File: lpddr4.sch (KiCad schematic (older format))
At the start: 90 parts, among them U1 MT53D1024M32D4DT-053, U3 MT53D1024M32D4DT-053

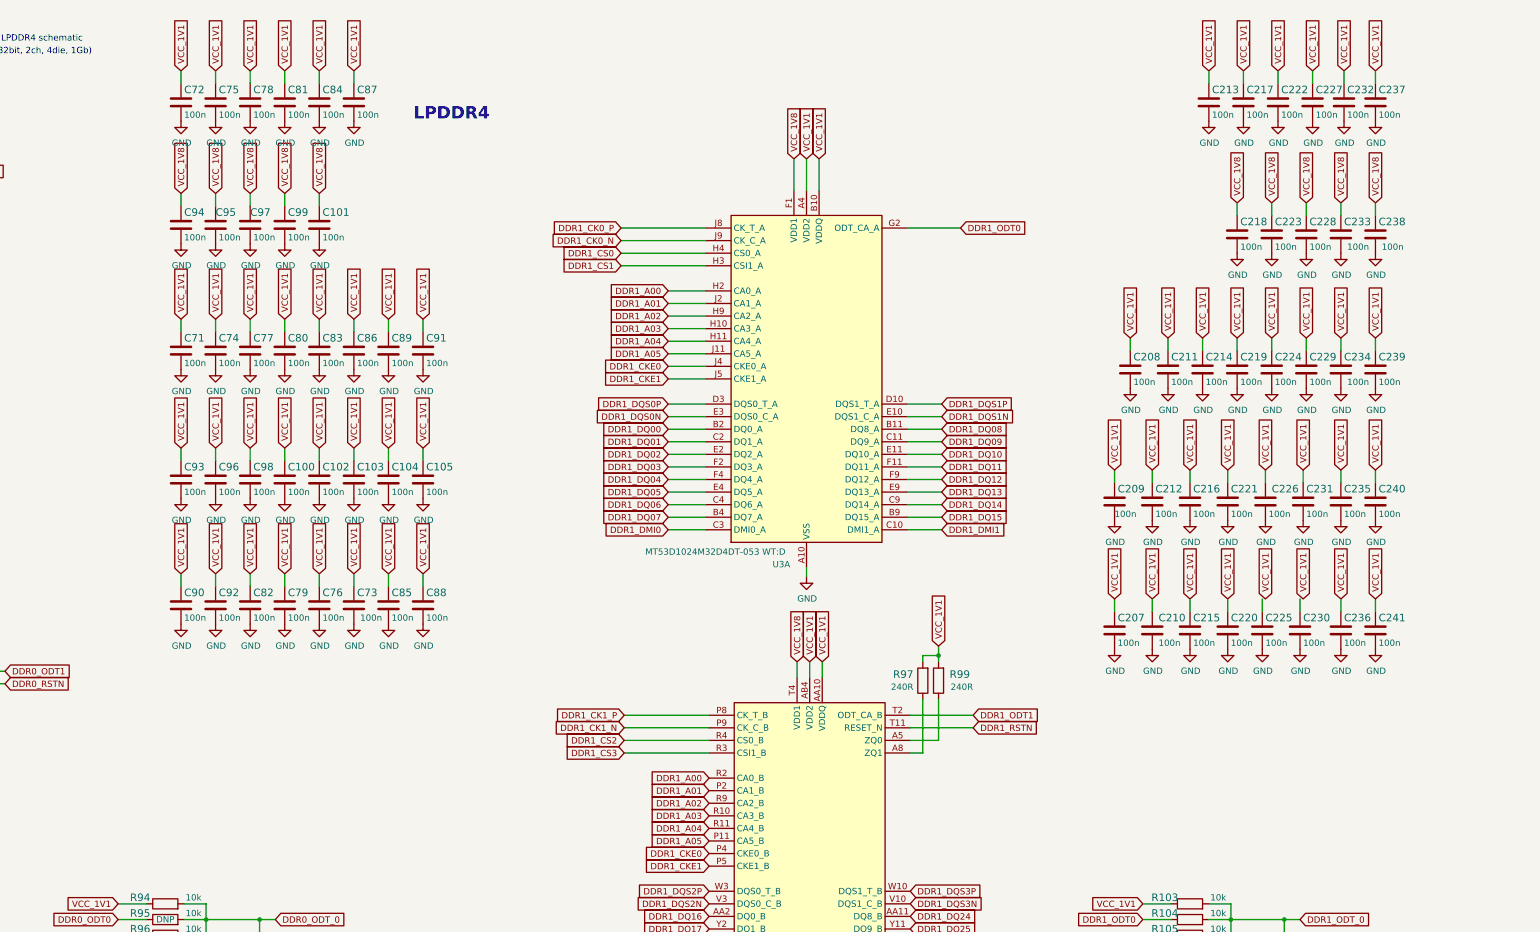
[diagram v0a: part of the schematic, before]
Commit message: Updated component placement - DDR decoupling done
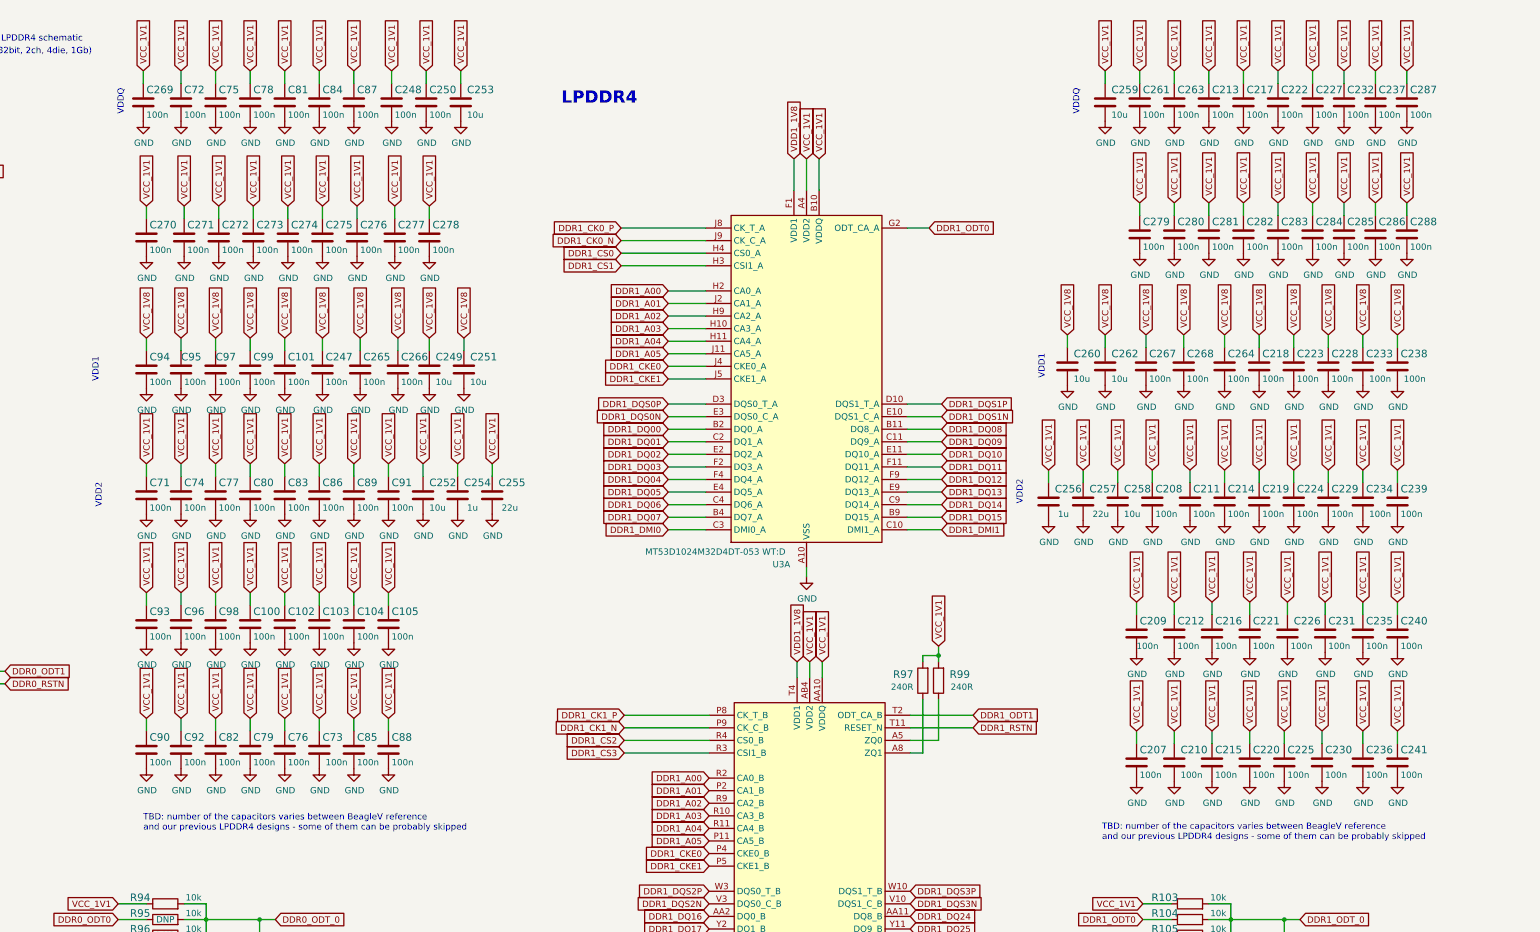
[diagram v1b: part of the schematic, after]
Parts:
- added C247, C248, C250, C261, C263, C264, C265, C266, C267, C268, C269, C270, C271, C272, C273, C274, C275, C276, C277, C278, C279, C280, C281, C282, C283, C284, C285, C286, C287, C288: C_100n_0201, arvsom-footprints:0201-res, symbol arvsom:C_100n_0201
- added C249, C251, C252, C253, C258, C259, C260, C262: C_10u_0402, arvsom-footprints:0402-cap, symbol arvsom:C_10u_0402
- added C254, C256: C_1u_0402, arvsom-footprints:0402-cap, symbol arvsom:C_1u_0402
- added C255, C257: C_22u_0603, arvsom-footprints:0603-cap, symbol arvsom:C_22u_0603
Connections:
- net GND: now also C247.2, C248.2, C249.2, C250.2, C251.2, C252.2, C253.2, C254.2, C255.2, C256.2, C257.2, C258.2, C259.2, C260.2, C261.2, C262.2, C263.2, C264.2, C265.2, C266.2, C267.2, C268.2, C269.2, C270.2, C271.2, C272.2, C273.2, C274.2, C275.2, C276.2, C277.2, C278.2, C279.2, C280.2, C281.2, C282.2, C283.2, C284.2, C285.2, C286.2, C287.2, C288.2
- net VCC_1V1: now also C225.1, C230.1, C248.1, C250.1, C252.1, C253.1, C254.1, C255.1, C256.1, C257.1, C258.1, C259.1, C261.1, C263.1, C269.1, C270.1, C271.1, C272.1, C273.1, C274.1, C275.1, C276.1, C277.1, C278.1, C279.1, C280.1, C281.1, C282.1, C283.1, C284.1, C285.1, C286.1, C287.1, C288.1
- net VCC_1V8: now also C247.1, C249.1, C251.1, C260.1, C262.1, C264.1, C265.1, C266.1, C267.1, C268.1; no longer U3.F1 (VDD1), U3.F12 (VDD1), U3.G4 (VDD1), U3.G9 (VDD1), U3.T4 (VDD1), U3.T9 (VDD1), U3.U1 (VDD1), U3.U12 (VDD1)
- new net VDD1_1V8: U3.F1 (VDD1), U3.F12 (VDD1), U3.G4 (VDD1), U3.G9 (VDD1), U3.T4 (VDD1), U3.T9 (VDD1), U3.U1 (VDD1), U3.U12 (VDD1)
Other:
- note added: "TBD: number of the capacitors varies between BeagleV reference\nand our previous LPDDR4 designs - some of them can be probably skipped"
- note added: "VDD1"
- note added: "VDD2"
- note added: "VDDQ"
- moved on the sheet: C100, C101, C102, C103, C104, C105, C207, C208, C209, C210, C211, C212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

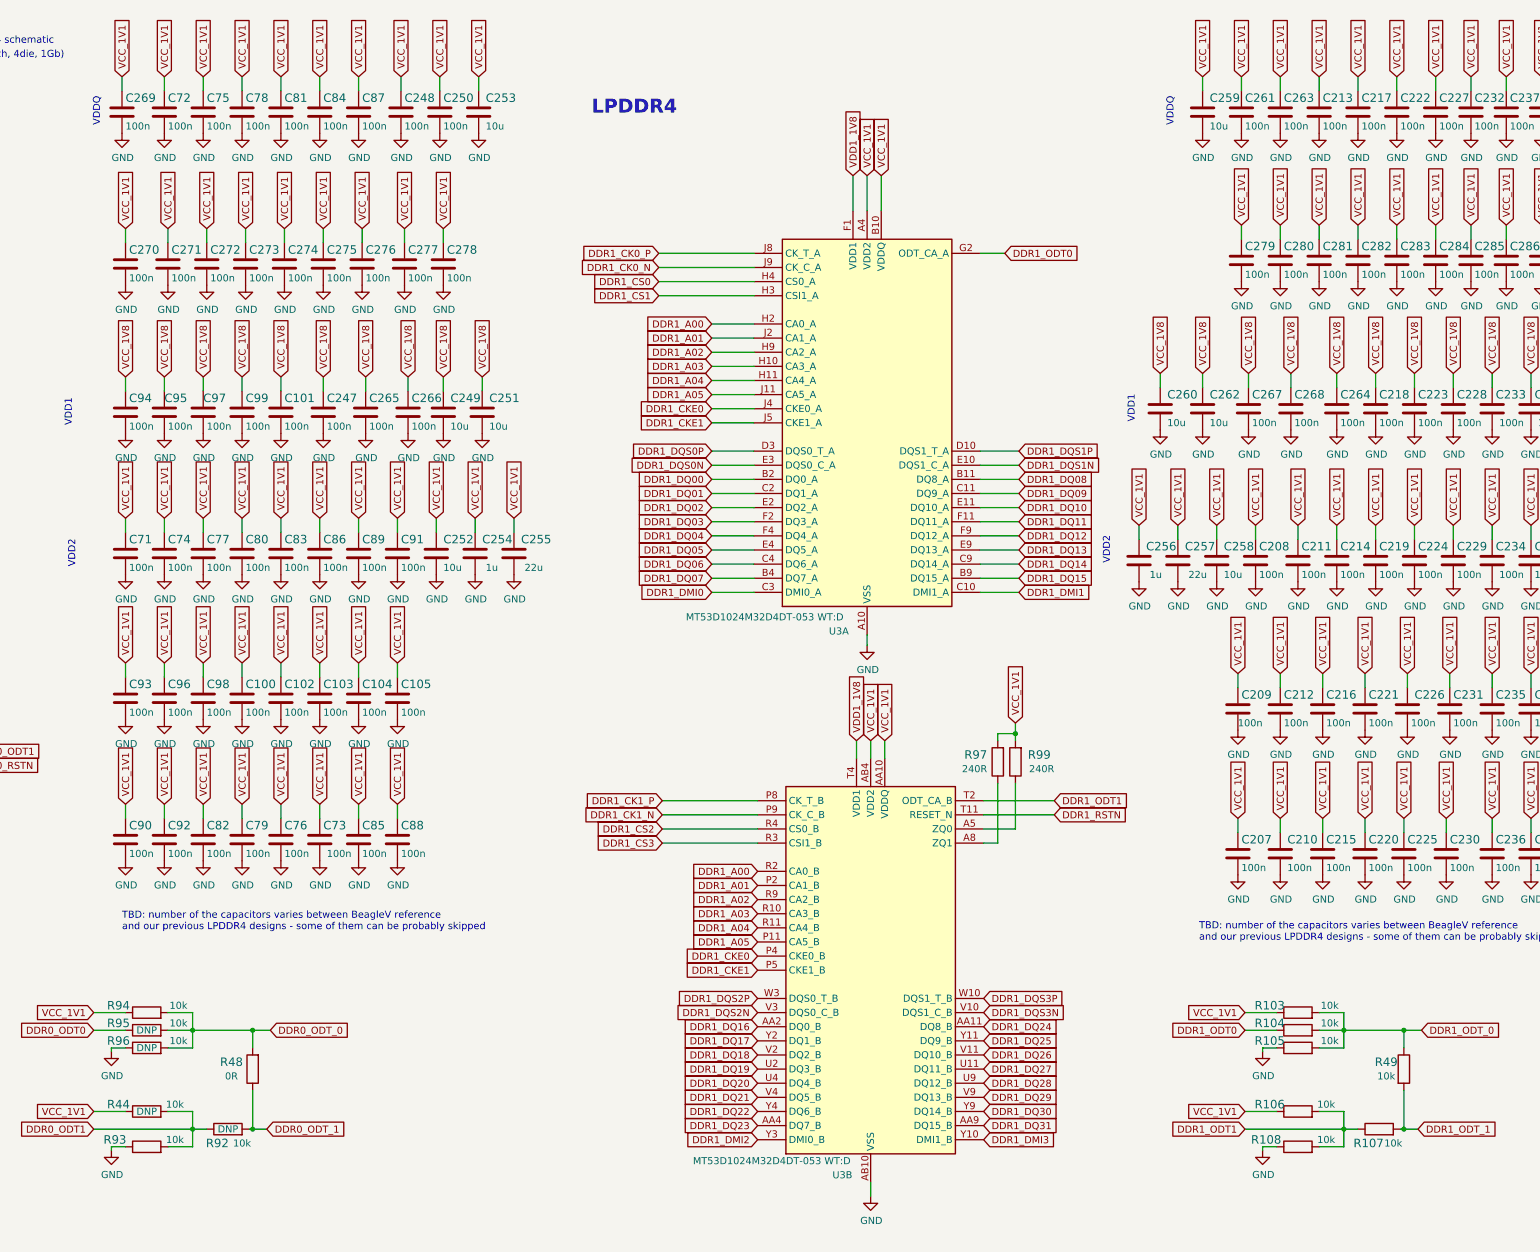
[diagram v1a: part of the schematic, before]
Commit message: Finished component placement
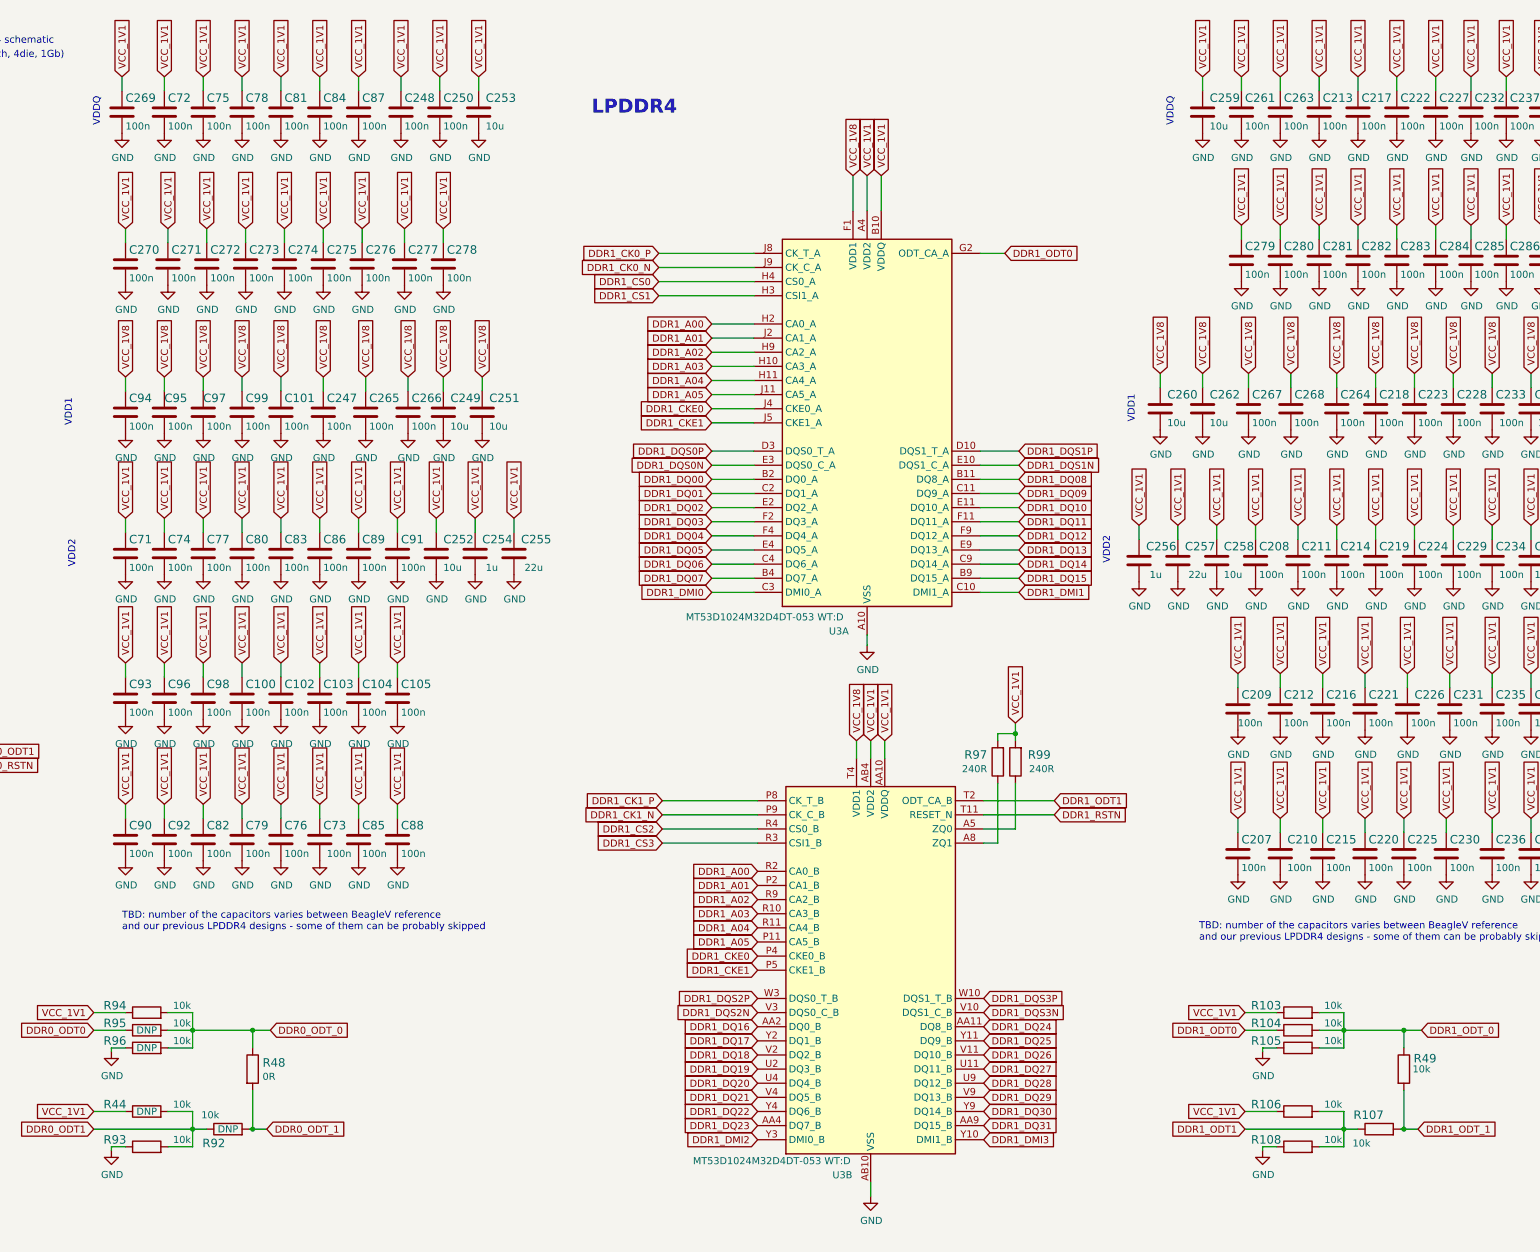
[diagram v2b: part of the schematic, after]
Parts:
- removed R103, R104, R105, R106, R107, R108, R44, R49, R92, R93, R94, R95, R96: R_10k_0402, arvsom-footprints:0402-res, symbol arvsom:R_10k_0402
- removed R48: R_0R_0402, arvsom-footprints:0402-res, symbol arvsom:R_0R_0402
- added R103, R104, R105, R106, R107, R108, R44, R49, R92, R93, R94, R95, R96: R_10k_0201, arvsom-footprints:0201-res, symbol arvsom:R_10k_0201
- added R48: R_0R_0201, arvsom-footprints:0201-res, symbol arvsom:R_0R_0201
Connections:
- net VDD1_1V8 is gone; now on net VCC_1V8: U3.F1 (VDD1), U3.F12 (VDD1), U3.G4 (VDD1), U3.G9 (VDD1), U3.T4 (VDD1), U3.T9 (VDD1), U3.U1 (VDD1), U3.U12 (VDD1)
- net DDR0_ODT0: now also R95.1
- net DDR0_ODT1: now also R44.2, R92.1, R93.2
- net DDR0_ODT_0: now also R48.1, R94.2, R95.2, R96.2
- net DDR0_ODT_1: now also R48.2, R92.2
- net DDR1_ODT0: now also R104.1
- net DDR1_ODT1: now also R106.2, R107.1, R108.2
- net DDR1_ODT_0: now also R103.2, R104.2, R105.2, R49.1
- net DDR1_ODT_1: now also R107.2, R49.2
- net GND: now also R105.1, R108.1, R93.1, R96.1
- net VCC_1V1: now also R103.1, R106.1, R44.1, R94.1
